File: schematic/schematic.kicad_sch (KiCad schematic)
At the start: 11 parts

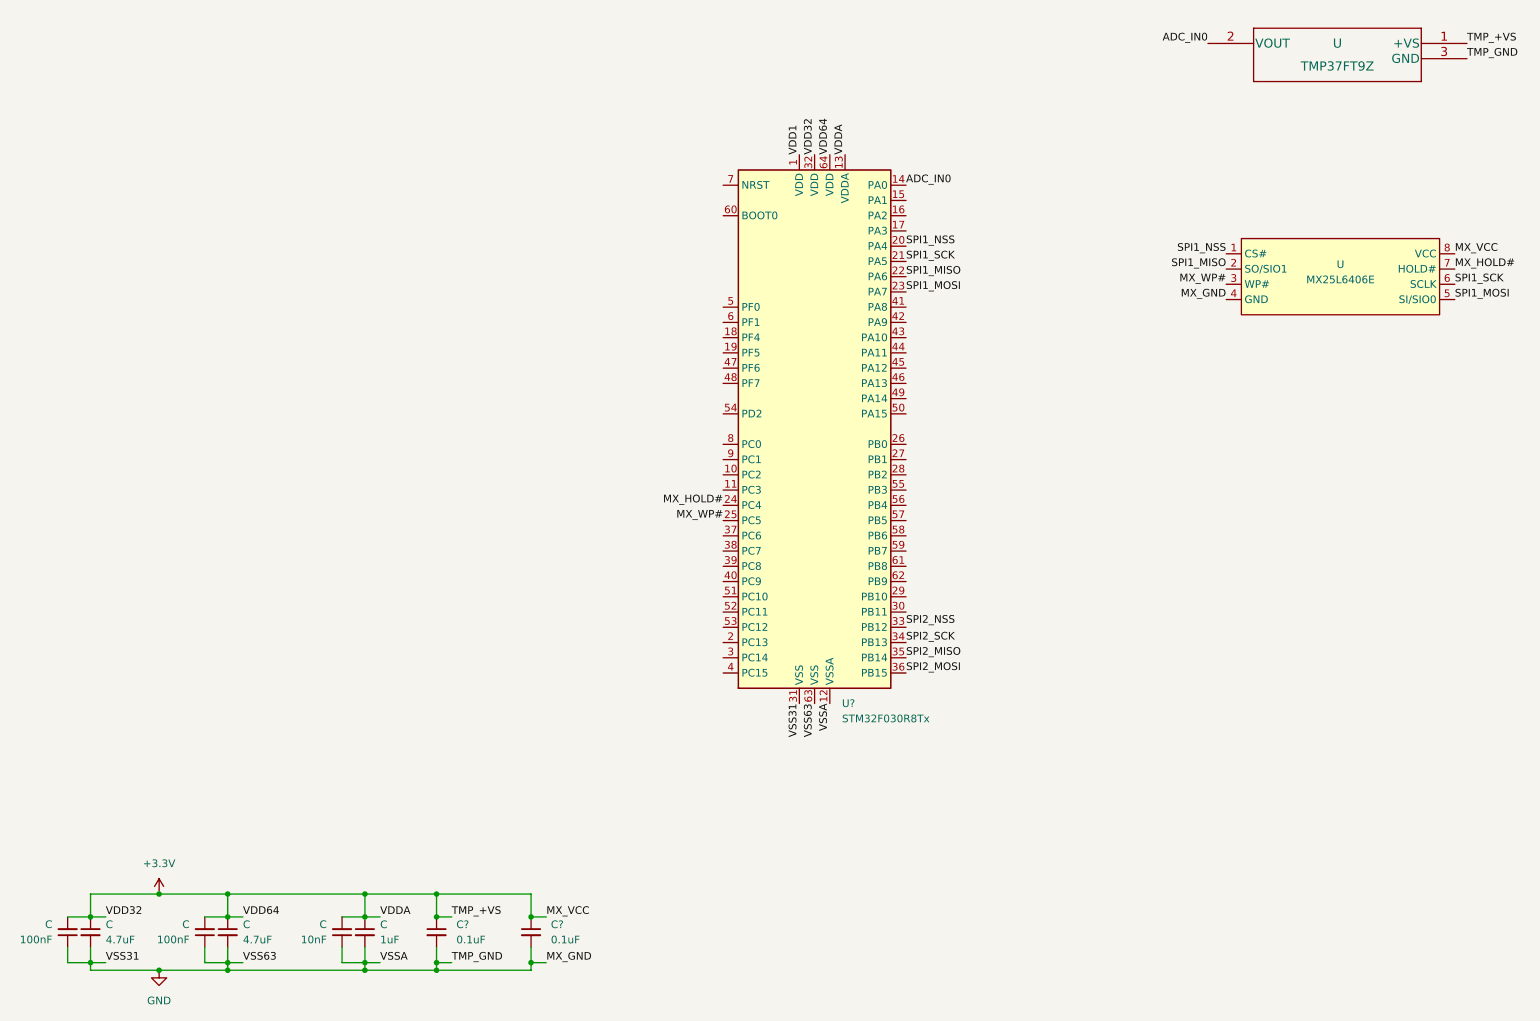
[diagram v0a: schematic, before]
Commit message: Chore added SD card library
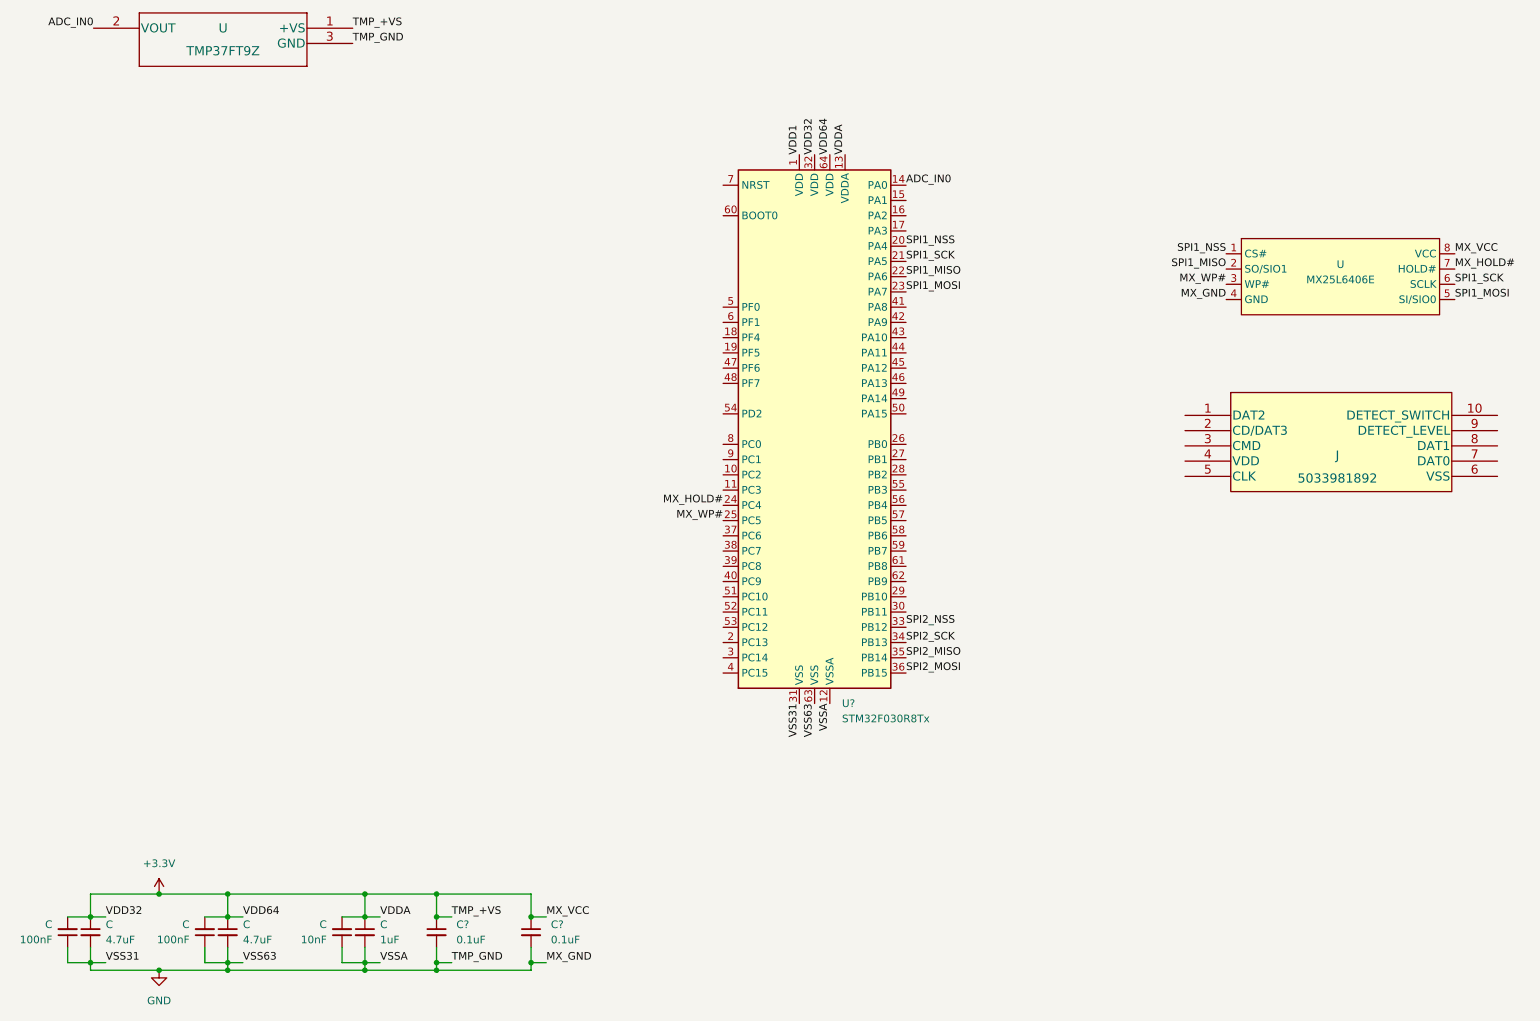
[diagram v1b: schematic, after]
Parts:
- added J: 5033981892, 503398-1892_MOL, symbol SD_5033981892:5033981892
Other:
- moved on the sheet: U
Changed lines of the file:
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@@
     (effects (font (size 1.27 1.27)) (justify left bottom))
   )
-  (label "TMP_GND" (at 256.032 36.068 0)
+  (label "TMP_GND" (at 70.358 33.528 0)
     (effects (font (size 1.27 1.27)) (justify left bottom))
   )
@@
     (effects (font (size 1.27 1.27)) (justify left bottom))
   )
-  (label "ADC_IN0" (at 212.852 33.528 180)
+  (label "ADC_IN0" (at 27.178 30.988 180)
     (effects (font (size 1.27 1.27)) (justify right bottom))
   )
@@
     (effects (font (size 1.27 1.27)) (justify left bottom))
   )
-  (label "TMP_+VS" (at 256.032 33.528 0)
+  (label "TMP_+VS" (at 70.358 30.988 0)
     (effects (font (size 1.27 1.27)) (justify left bottom))
   )
@@
     (pin "1")
     (pin "2")
+  )
+  (symbol (lib_id "SD_5033981892:5033981892") (at 209.042 95.504 0) (unit 1)
+    (in_bom yes) (on_board yes)
+    (property "Reference" "J" (id 0) (at 234.442 102.1836 0)
+      (effects (font (size 1.524 1.524)))
+    )
+    (property "Value" "5033981892" (id 1) (at 234.442 105.9936 0)
+      (effects (font (size 1.524 1.524)))
+    )
+    (property "Footprint" "503398-1892_MOL" (id 2) (at 235.712 89.154 0)
+      (effects (font (size 1.524 1.524)) hide)
+    )
+    (property "Datasheet" "" (id 3) (at 209.042 95.504 0)
+      (effects (font (size 1.524 1.524)))
+    )
+    (pin "1")
+    (pin "10")
+    (pin "2")
+    (pin "3")
+    (pin "4")
+    (pin "5")
+    (pin "6")
+    (pin "7")
+    (pin "8")
+    (pin "9")
   )
   (symbol (lib_id "Device:C_Small") (at 84.328 181.61 0) (unit 1)
@@
     (pin "9")
   )
-  (symbol (lib_id "TMP37FT9Z:TMP37FT9Z") (at 200.152 36.068 0) (unit 1)
+  (symbol (lib_id "TMP37FT9Z:TMP37FT9Z") (at 14.478 33.528 0) (unit 1)
     (in_bom yes) (on_board yes)
-    (property "Reference" "U" (id 0) (at 234.442 33.528 0)
-      (effects (font (size 1.524 1.524)))
-    )
-    (property "Value" "TMP37FT9Z" (id 1) (at 234.442 37.338 0)
-      (effects (font (size 1.524 1.524)))
-    )
-    (property "Footprint" "T_3_ADI" (id 2) (at 234.442 29.718 0)
+    (property "Reference" "U" (id 0) (at 48.768 30.988 0)
+      (effects (font (size 1.524 1.524)))
+    )
+    (property "Value" "TMP37FT9Z" (id 1) (at 48.768 34.798 0)
+      (effects (font (size 1.524 1.524)))
+    )
+    (property "Footprint" "T_3_ADI" (id 2) (at 48.768 27.178 0)
       (effects (font (size 1.524 1.524)) hide)
     )
-    (property "Datasheet" "" (id 3) (at 256.032 33.528 0)
+    (property "Datasheet" "" (id 3) (at 70.358 30.988 0)
       (effects (font (size 1.524 1.524)))
     )
@@
       (reference "C?") (unit 1) (value "0.1uF") (footprint "")
     )
+    (path "/6548fff9-e3a8-4a8d-8791-5da239638f8c"
+      (reference "J") (unit 1) (value "5033981892") (footprint "503398-1892_MOL")
+    )
     (path "/ec8b09ca-6420-470b-a21a-f5741860ec5a"
